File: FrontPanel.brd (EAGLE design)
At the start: 100 x 61 mm, 28 parts, among them U1 TPIC6B595N, U2 TPIC6B595N, U3 TPIC6B595N, U4 TPIC6B595N, U5 TPIC6B595N, U6 TPIC6B595N

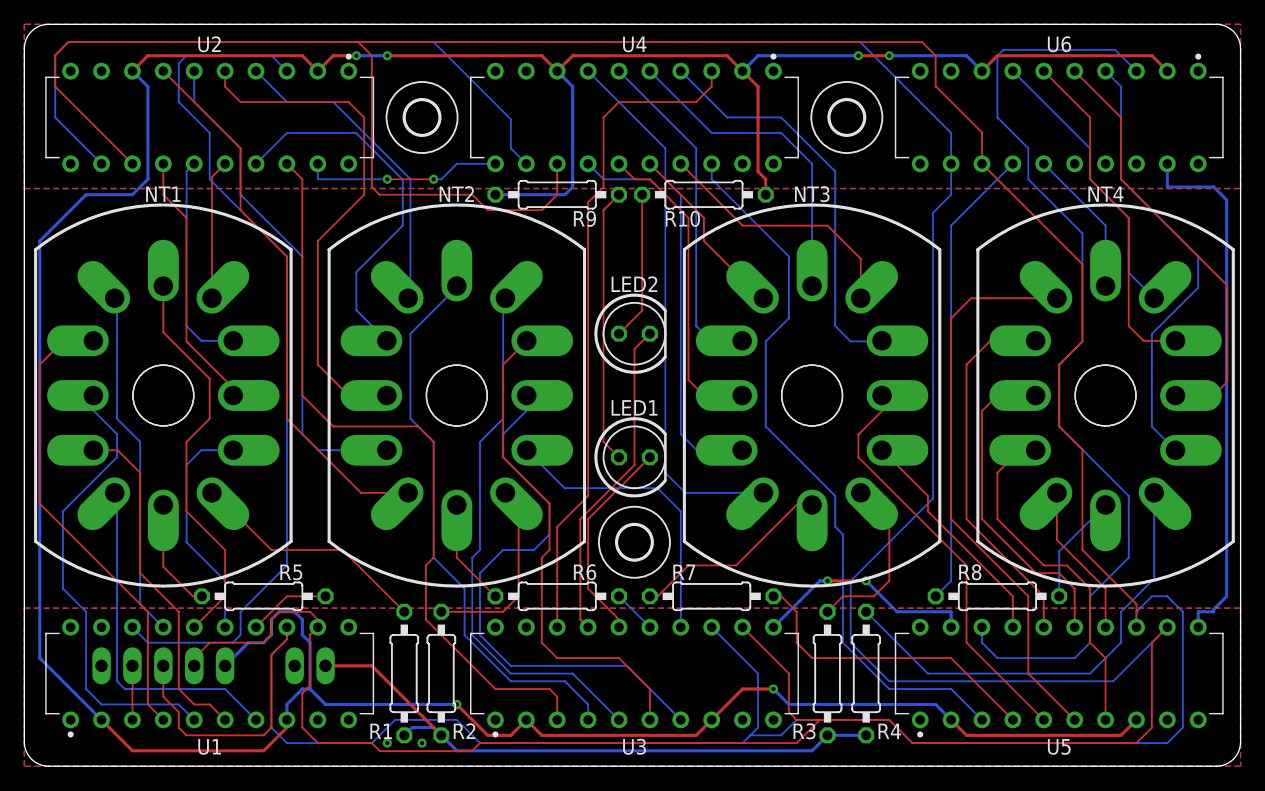
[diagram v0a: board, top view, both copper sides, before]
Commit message: switched to smd LEDs and added Light-Pipes
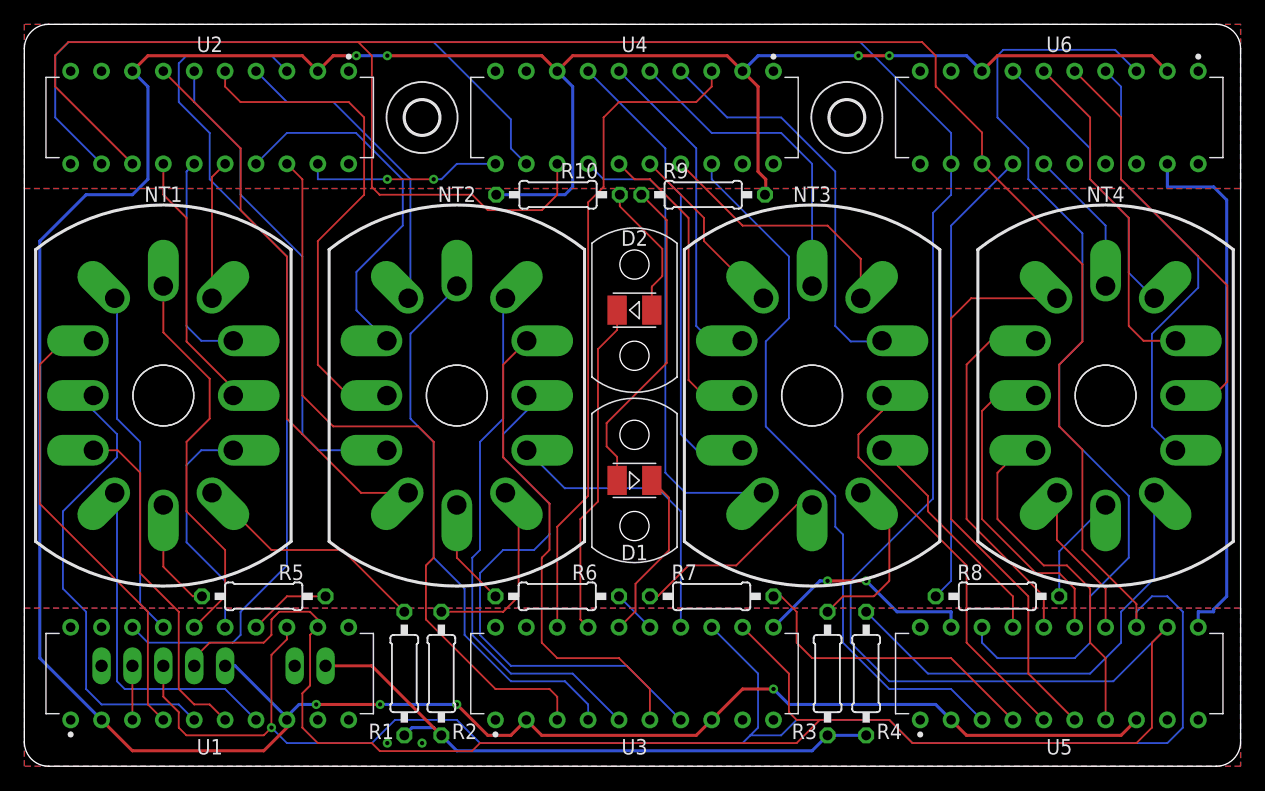
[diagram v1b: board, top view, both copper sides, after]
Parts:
- removed LED1, LED2: (no value), led:LED5MM
- removed U$3: (no value), holes:2,8
- added D1, D2: (no value), Wurth_Elektronik_Optoelectronics_rev17b:WL-SMTW_3528
- added U$5, U$6: (no value), NixieClock:MENTOR-1216.1005
- moved U$4 26.8 mm to (23.2, 44.2)
- moved R10 12.0 mm to (43.9, 47.0), turned to 180 degrees
- moved R9 12.0 mm to (55.8, 47.0), turned to 0 degrees
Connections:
- net LED1: now also D1.1; no longer LED1.K
- net LED2: now also D2.1; no longer LED2.K
- net N$66: now also D1.2; no longer LED1.A
- net N$67: now also D2.2; no longer LED2.A
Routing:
- net +5V: track 290.7 -> 280.9 mm, vias 6 -> 8
- net SCLK: track 308.6 -> 299.8 mm, vias 0 -> 1
- net N$66: track 22.6 -> 26.8 mm
- net LED1: track 17.1 -> 14.4 mm
- net N$67: track 12.2 -> 11.3 mm
- net LED2: track 26.8 -> 27.6 mm
